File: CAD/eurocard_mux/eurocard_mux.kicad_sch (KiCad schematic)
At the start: 28 parts, among them J1 1759091, J10 T812112A101CEU, J11 971150321, J12 971150321, J13 971150321, J14 971150321, J2 1759091, J3 MC-254-12-00-RA-DIP, J4 MC-254-12-00-RA-DIP, J5 1759091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

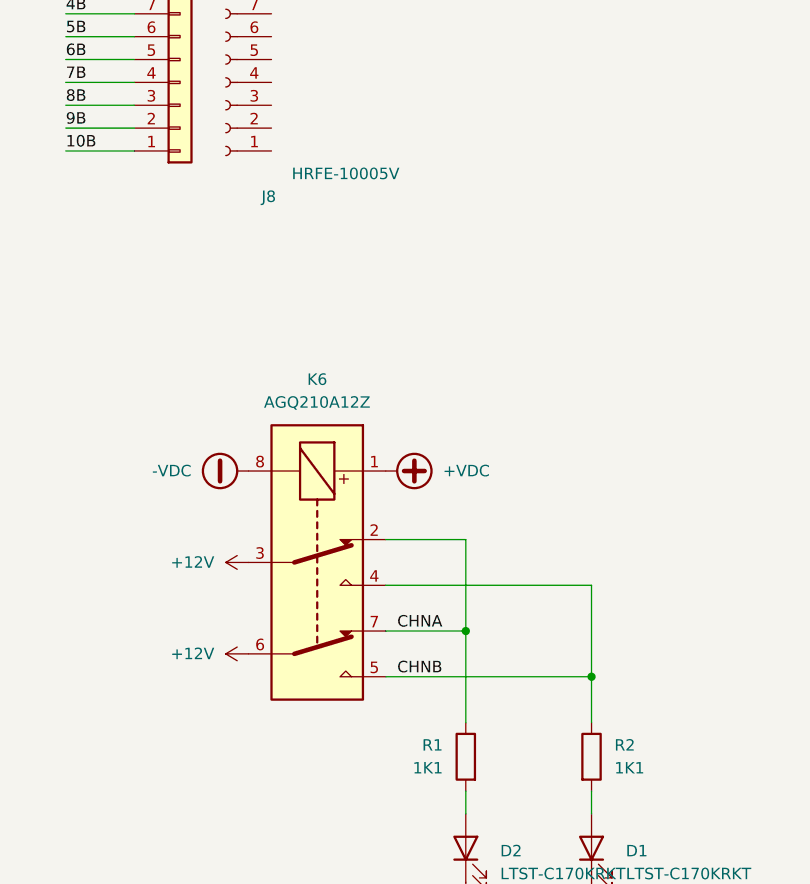
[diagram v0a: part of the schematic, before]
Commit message: Switched let connections for correct id
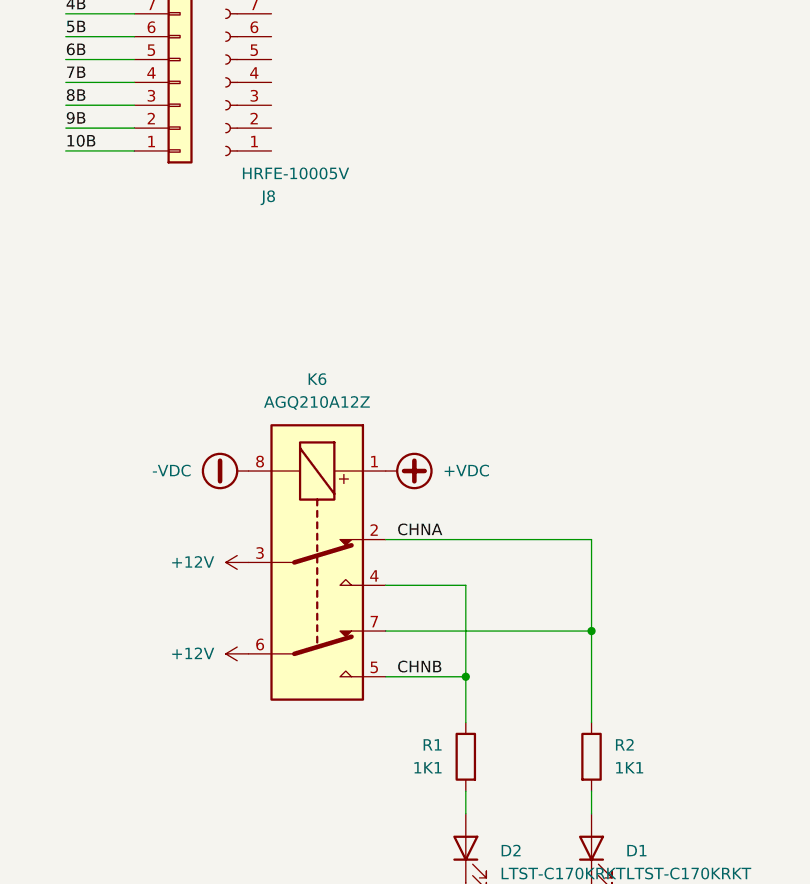
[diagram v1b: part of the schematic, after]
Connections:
- net CHNA: now also R2.1; no longer R1.1
- net CHNB: now also R1.1; no longer R2.1
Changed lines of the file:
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@@
 		(title "SPI-MUX")
 		(date "2023-02-06")
-		(rev "1.0.1")
+		(rev "1.0.3")
 		(company "NMBU-Mina")
 		(comment 1 "F.N.Beilegaard")
 	)
 	(junction
-		(at 279.4 234.95)
+		(at 265.43 234.95)
 		(diameter 0)
 		(color 0 0 0 0)
@@
 	)
 	(junction
-		(at 353.06 113.03)
+		(at 279.4 229.87)
 		(diameter 0)
 		(color 0 0 0 0)
 	)
 	(junction
-		(at 265.43 229.87)
+		(at 353.06 113.03)
 		(diameter 0)
 		(color 0 0 0 0)
@@
 	(wire
 		(pts
-			(xy 201.93 76.2) (xy 228.6 76.2)
+			(xy 265.43 234.95) (xy 265.43 240.03)
 		)
 		(stroke
@@
 	(wire
 		(pts
-			(xy 256.54 229.87) (xy 265.43 229.87)
+			(xy 201.93 76.2) (xy 228.6 76.2)
 		)
 		(stroke
@@
 	(wire
 		(pts
-			(xy 265.43 219.71) (xy 265.43 229.87)
-		)
-		(stroke
-			(width 0)
-			(type default)
-		)
-	)
-	(wire
-		(pts
 			(xy 86.36 63.5) (xy 157.48 63.5)
 		)
@@
 	(wire
 		(pts
-			(xy 279.4 234.95) (xy 279.4 240.03)
+			(xy 279.4 229.87) (xy 279.4 240.03)
 		)
 		(stroke
@@
 	(wire
 		(pts
+			(xy 256.54 219.71) (xy 279.4 219.71)
+		)
+		(stroke
+			(width 0)
+			(type default)
+		)
+	)
+	(wire
+		(pts
 			(xy 172.72 187.96) (xy 204.47 187.96)
 		)
@@
 	(wire
 		(pts
-			(xy 220.98 171.45) (xy 228.6 171.45)
+			(xy 256.54 234.95) (xy 265.43 234.95)
 		)
 		(stroke
@@
 	(wire
 		(pts
-			(xy 172.72 148.59) (xy 199.39 148.59)
+			(xy 220.98 171.45) (xy 228.6 171.45)
 		)
 		(stroke
@@
 	(wire
 		(pts
-			(xy 220.98 163.83) (xy 228.6 163.83)
+			(xy 172.72 148.59) (xy 199.39 148.59)
 		)
 		(stroke
@@
 	(wire
 		(pts
-			(xy 153.67 66.04) (xy 153.67 73.66)
+			(xy 220.98 163.83) (xy 228.6 163.83)
 		)
 		(stroke
@@
 	(wire
 		(pts
-			(xy 256.54 224.79) (xy 279.4 224.79)
+			(xy 153.67 66.04) (xy 153.67 73.66)
 		)
 		(stroke
@@
 	(wire
 		(pts
-			(xy 256.54 219.71) (xy 265.43 219.71)
+			(xy 265.43 224.79) (xy 265.43 234.95)
 		)
 		(stroke
@@
 	(wire
 		(pts
-			(xy 279.4 224.79) (xy 279.4 234.95)
+			(xy 279.4 219.71) (xy 279.4 229.87)
 		)
 		(stroke
@@
 	(wire
 		(pts
+			(xy 256.54 229.87) (xy 279.4 229.87)
+		)
+		(stroke
+			(width 0)
+			(type default)
+		)
+	)
+	(wire
+		(pts
 			(xy 199.39 73.66) (xy 228.6 73.66)
 		)
@@
 	(wire
 		(pts
-			(xy 256.54 234.95) (xy 279.4 234.95)
+			(xy 265.43 224.79) (xy 256.54 224.79)
 		)
 		(stroke
@@
 	(wire
 		(pts
-			(xy 265.43 229.87) (xy 265.43 240.03)
-		)
-		(stroke
-			(width 0)
-			(type default)
-		)
-	)
-	(wire
-		(pts
 			(xy 365.76 118.11) (xy 365.76 115.57)
 		)
@@
 	)
 	(label "CHNA"
-		(at 257.81 229.87 0)
+		(at 257.81 219.71 0)
 		(effects
 			(font
@@
 		)
 		(property "Value" "HRFE-10005V"
-			(at 258.064 179.07 0)
+			(at 252.476 179.07 0)
 			(effects
 				(font
